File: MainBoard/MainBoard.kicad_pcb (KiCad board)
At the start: 6 copper layers, 45 x 44 mm, 114 parts, among them J2 USB4110-GF-A, J3 M55-7104042R, J4 Conn_01x04_Pin, J5 Conn_01x02_Pin, Q1 PMV19XNEAR, Q2 PMV19XNEAR, Q3 PMV19XNEAR, Q4 PMV19XNEAR, SW1 SW_TL1015AF160QG, SW2 SW_TL1015AF160QG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

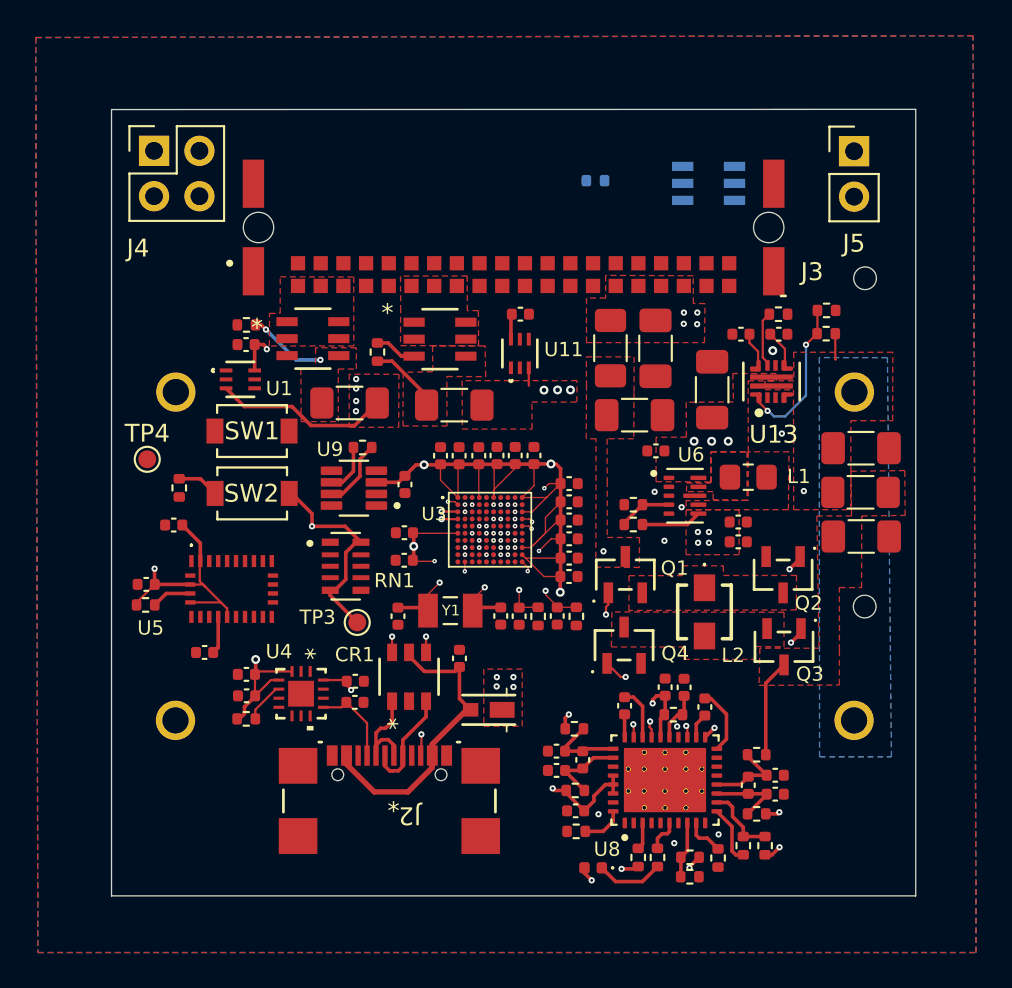
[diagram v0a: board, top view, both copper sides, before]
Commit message: Pushing BOM and changes
Had to change one resistor footprint and routing
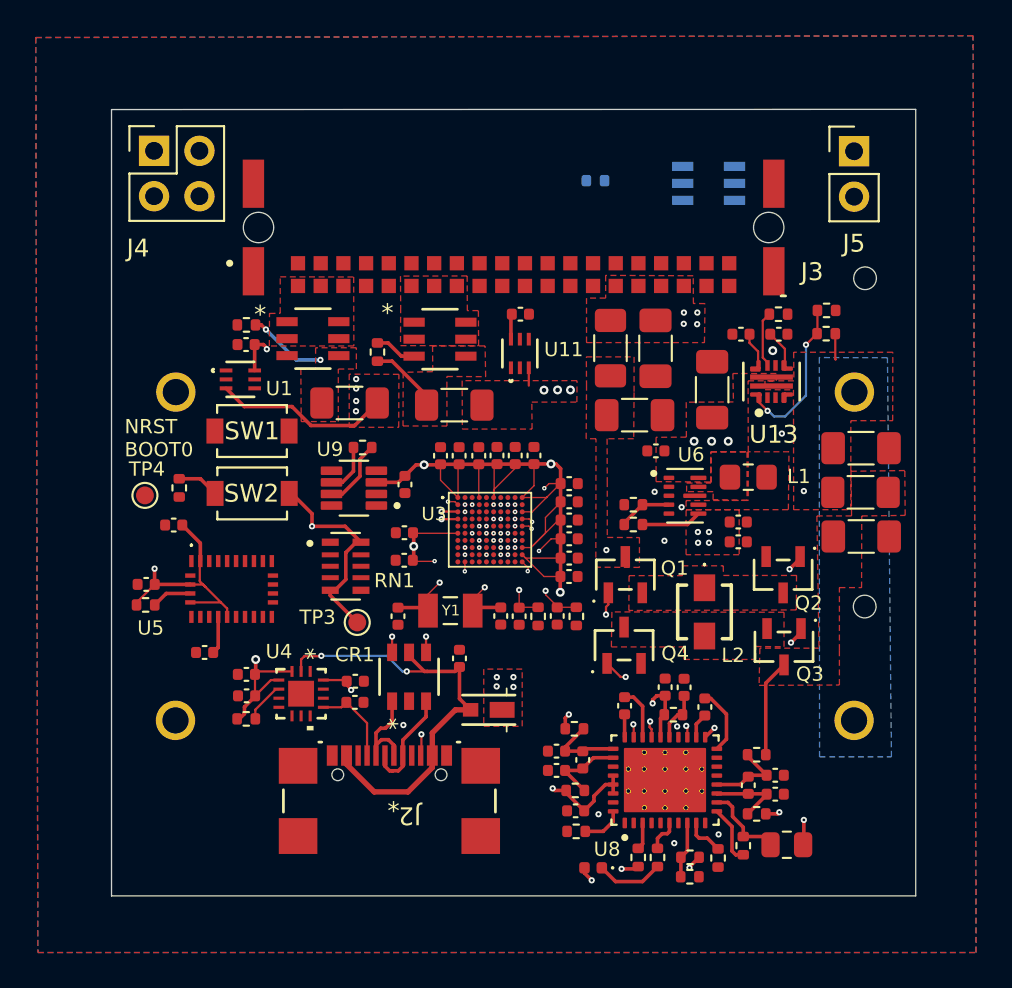
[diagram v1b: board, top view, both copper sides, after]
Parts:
- R15: footprint Resistor_SMD:R_0402_1005Metric -> Resistor_SMD:R_0805_2012Metric
- moved TP4 2.02 mm to (71.3, 63.4)
- moved R15 1.22 mm to (107.2, 82.9), turned to 0 degrees
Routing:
- net Net-(D1-A): track 16.9 -> 25.4 mm, vias 0 -> 2
- net BAT+: track 24.1 -> 25.1 mm
- net GND: vias 15 -> 16
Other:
- board text added: "3.3V GND"
- board text added: "JTCK/SWCLK JTMS/SWDIO NRST SWO"
- board text added: "NRST BOOT0"

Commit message: Routing
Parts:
- moved R3 3.64 mm to (109.0, 50.7)
- moved R4 3.41 mm to (109.0, 49.6), turned to 0 degrees
- moved R35 2.19 mm to (98.5, 45.0)
- moved R5 1.40 mm to (105.5, 53.9), turned to -90 degrees
- moved R15 0.96 mm to (106.4, 83.5), turned to -90 degrees
- moved C48 0.82 mm to (103.8, 54.3)
- moved C49 0.49 mm to (106.6, 53.9), turned to -90 degrees
- moved C34 0.08 mm to (111.3, 65.6)
- renumbered TP3 to 3.3V, TP4 to GND
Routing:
- net I2C2_SDA: track 0.00 -> 58.2 mm, vias 0 -> 5
- net I2C2_SCL: track 0.00 -> 55.7 mm, vias 1 -> 6
- net I2C1_SDA: track 0.00 -> 51.7 mm, vias 0 -> 6
- net NRST: track 0.00 -> 45.1 mm, vias 1 -> 2
- net HEATER_ENABLE: track 0.00 -> 40.9 mm, vias 0 -> 4
- net I2C1_SCL: track 0.00 -> 40.9 mm, vias 1 -> 5
- net SWO: track 0.00 -> 37.3 mm, vias 1 -> 3
- net I2C4_SCL: track 0.00 -> 36.0 mm, vias 0 -> 6
- net JTMS/SWDIO: track 0.00 -> 34.9 mm, vias 1 -> 2
- net I2C3_SCL: track 0.00 -> 34.5 mm, vias 0 -> 4
- net JTCK/SWCLK: track 0.00 -> 33.7 mm, vias 1 -> 2
- net I2C4_SDA: track 0.00 -> 31.8 mm, vias 1 -> 5
- net ADC1_A1: track 0.00 -> 30.8 mm, vias 0 -> 3
- net CAN_L: track 2.81 -> 32.5 mm, vias 0 -> 3
- net CAN_H: track 3.89 -> 32.0 mm, vias 0 -> 3
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- added copper zone on B.Cu, net PROTECTED_VOLTAGE

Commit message: Routing updates
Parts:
- moved C48 0.69 mm to (104.3, 53.8), turned to -90 degrees
- moved 3.3V 0.16 mm to (83.3, 70.3)
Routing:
- net GND: track 1.74 -> 14.0 mm, vias 31 -> 34
- net NRST: track 45.1 -> 39.7 mm
- net JTCK/SWCLK: track 33.7 -> 32.2 mm, vias 2 -> 1
- net SWO: track 37.3 -> 38.3 mm, vias 3 -> 2
- net ADC1_A1: track 30.8 -> 31.3 mm
- net I2C4_SCL: track 36.0 -> 36.5 mm
- net JTMS/SWDIO: track 34.9 -> 35.4 mm, vias 2 -> 1

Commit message: More Routing
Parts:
- moved GND 23.6 mm to (94.6, 60.0)
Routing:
- net PARENT_SPI3_SCK: track 14.8 -> 17.8 mm

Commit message: Routing updates
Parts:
- moved C39 0.26 mm to (111.2, 60.5)
- moved R29 0.26 mm to (111.2, 63.0)
- moved C34 0.26 mm to (111.2, 65.4)
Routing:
- net CAN_L: track 32.5 -> 31.8 mm
- net CAN_H: track 32.0 -> 32.5 mm
- net GND: vias 34 -> 35

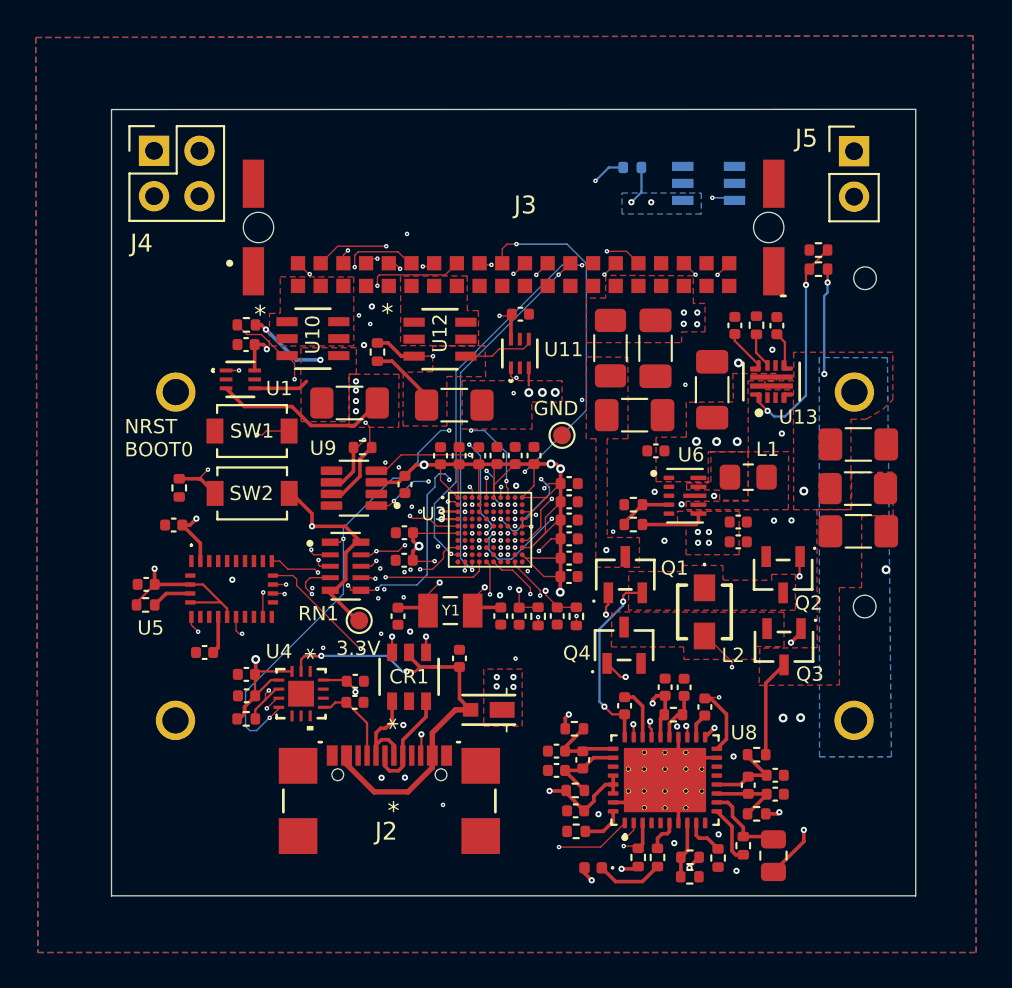
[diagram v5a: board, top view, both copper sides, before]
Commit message: Mounting pad additions, footswitch and BOM changes
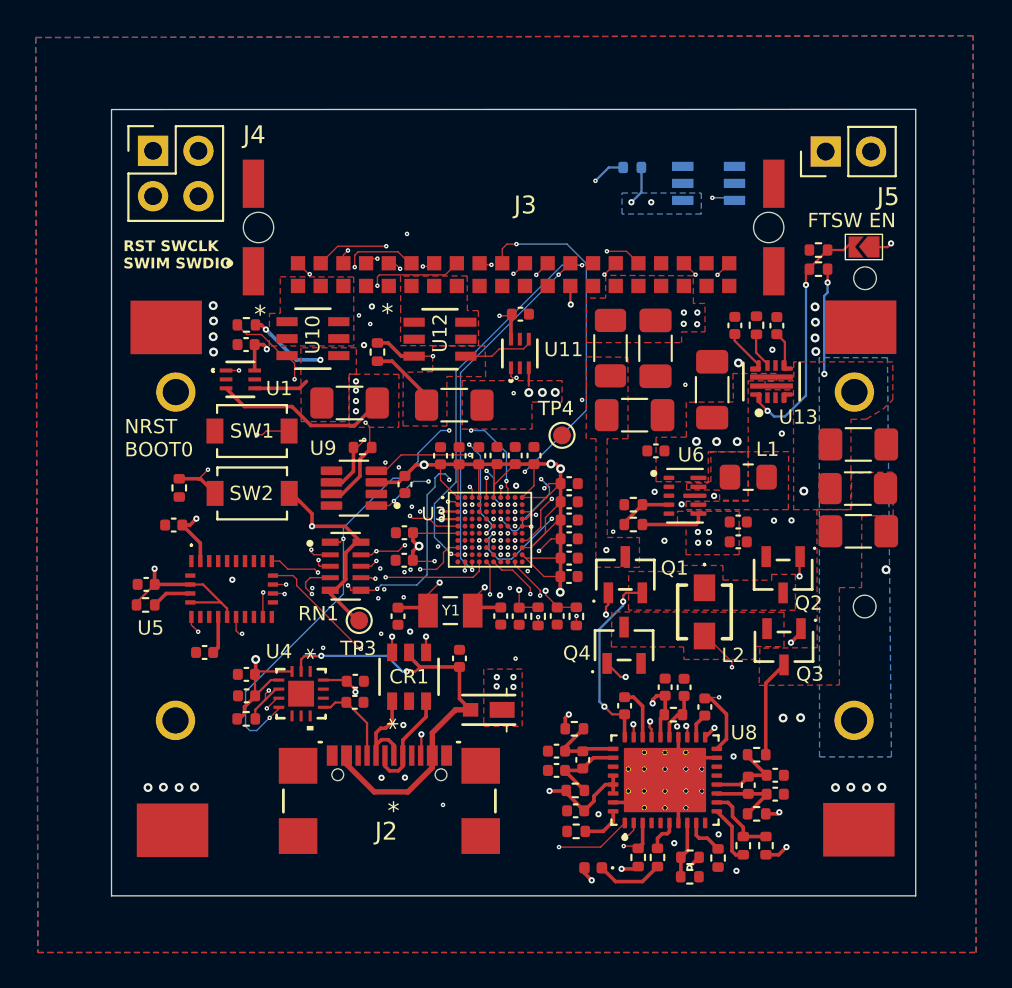
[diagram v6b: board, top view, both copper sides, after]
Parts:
- added H1: MountingHole_Pad, inspirefly:MoutingPad, F.Cu at (72.5, 54.1)
- added H2: MountingHole_Pad, inspirefly:MoutingPad, F.Cu at (111.4, 54.0)
- added H3: MountingHole_Pad, inspirefly:MoutingPad, F.Cu at (72.9, 82.2)
- added H4: MountingHole_Pad, inspirefly:MoutingPad, F.Cu at (111.3, 82.2)
- added JP1: FTSW EN, inspirefly:SmallJumper, F.Cu at (111.5, 49.4)
- R14: value 143k -> 82.5k
- R15: value 250k -> 143k; footprint Resistor_SMD:R_0805_2012Metric -> Resistor_SMD:R_0402_1005Metric
- moved J5 1.59 mm to (109.4, 44.1), turned to 90 degrees
- moved R15 0.70 mm to (106.0, 83.0)
- moved J4 0.06 mm to (71.7, 44.1)
- renumbered 3.3V to TP3, GND to TP4
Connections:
- J3 pad B13: unconnected-(J3-PadB13) -> FOOTSWITCH
- J4 pad 1: JTMS/SWDIO -> NRST
- J4 pad 4: NRST -> JTMS/SWDIO
- U3 pad F3: BAT_PULLDOWN -> unconnected-(U3A-PD14-PadF3)
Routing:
- net FOOTSWITCH: track 0.00 -> 21.8 mm, vias 0 -> 2
- net NRST: track 39.7 -> 43.6 mm
- net JTMS/SWDIO: track 35.4 -> 32.5 mm
- net JTCK/SWCLK: track 32.2 -> 34.5 mm
- net Net-(JP1-B): track 12.5 -> 14.1 mm
- net ADC1_A1: track 31.3 -> 30.7 mm
- net GND: track 14.0 -> 14.1 mm, vias 35 -> 51
- net BAT_PULLDOWN: vias 1 -> 0
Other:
- board text added: "+"
- board text added: "-"
- board text added: "GND +3.3V"
- board text added: "RST SWCLK SWIM SWDIO"
- board text removed: "3.3V GND"
- board text removed: "JTCK/SWCLK JTMS/SWDIO NRST SWO"
